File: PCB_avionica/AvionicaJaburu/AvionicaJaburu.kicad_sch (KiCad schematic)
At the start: 41 parts, among them J1 Screw_Terminal_01x02, J2 Screw_Terminal_01x02, J3 RESET, J4 Conn_01x08_Pin, J5 VDD, Q1 NMOS_Substrate, Q2 NMOS_Substrate, U1 AMS1117-3.3, U2 ESP32-DEVKIT-V1

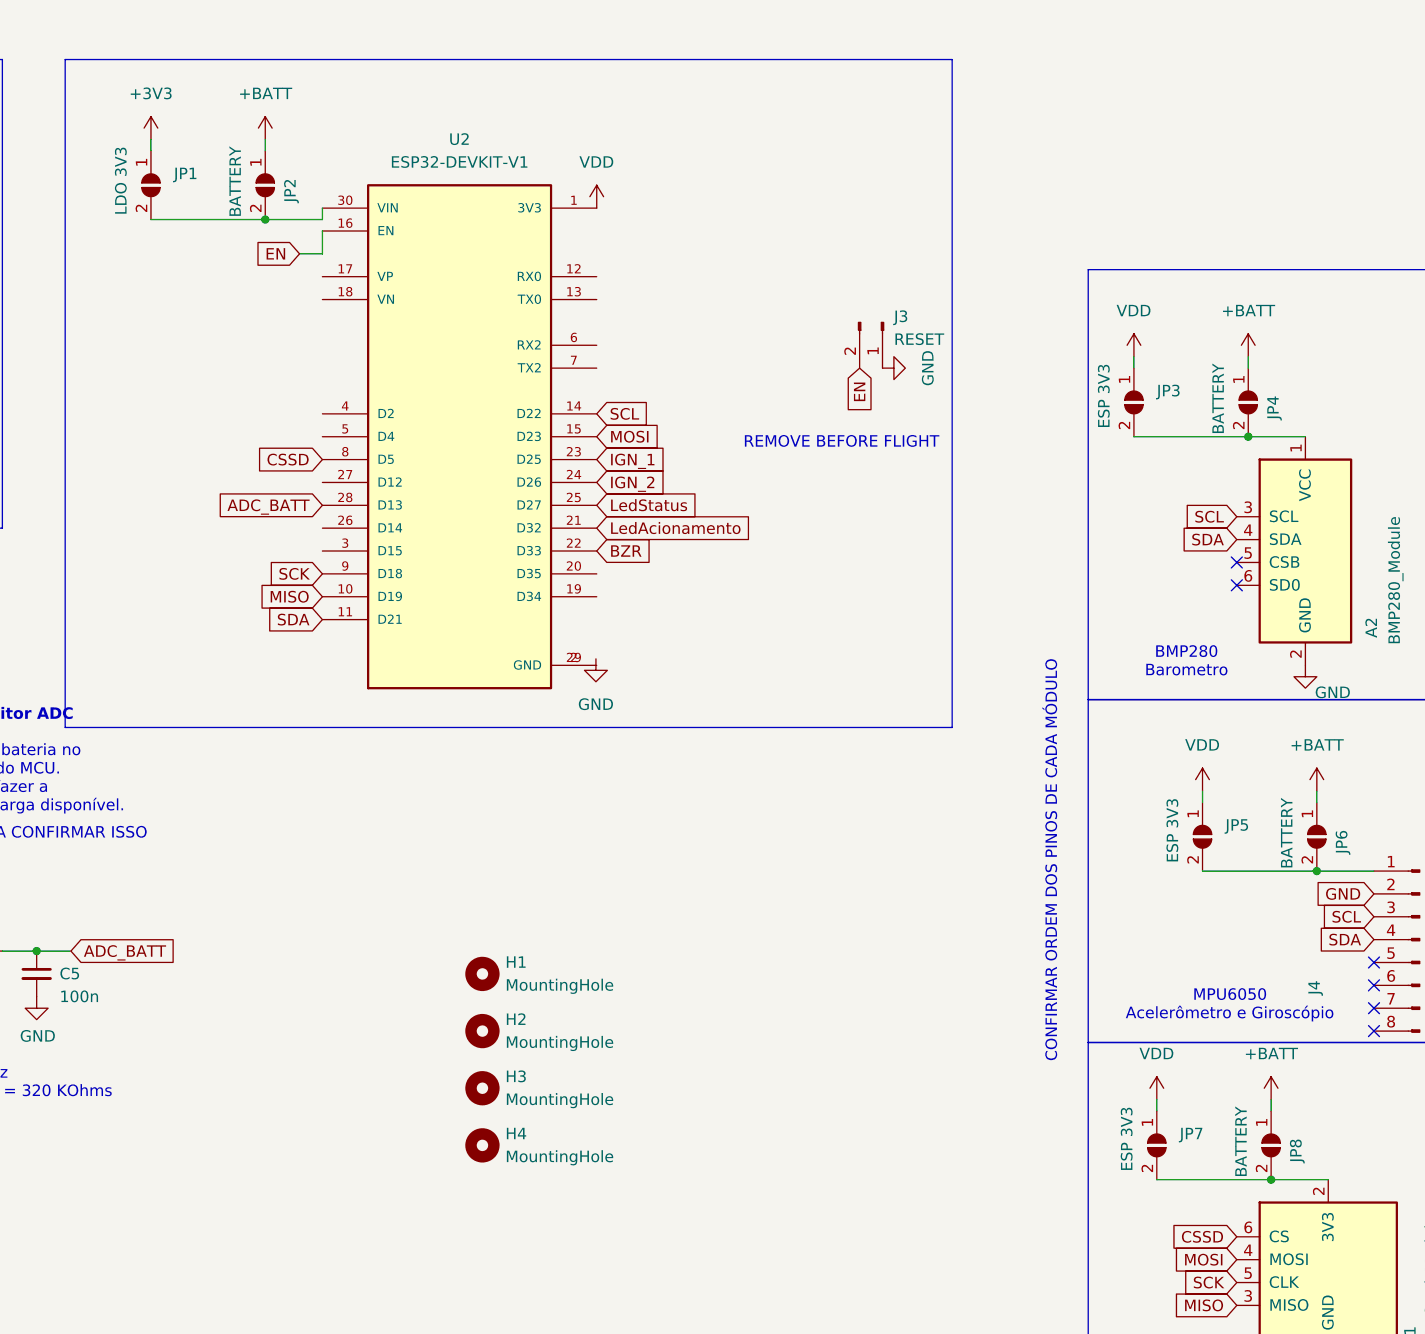
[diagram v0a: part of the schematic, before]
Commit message: outline da Jaburu corrigido pra fabricação
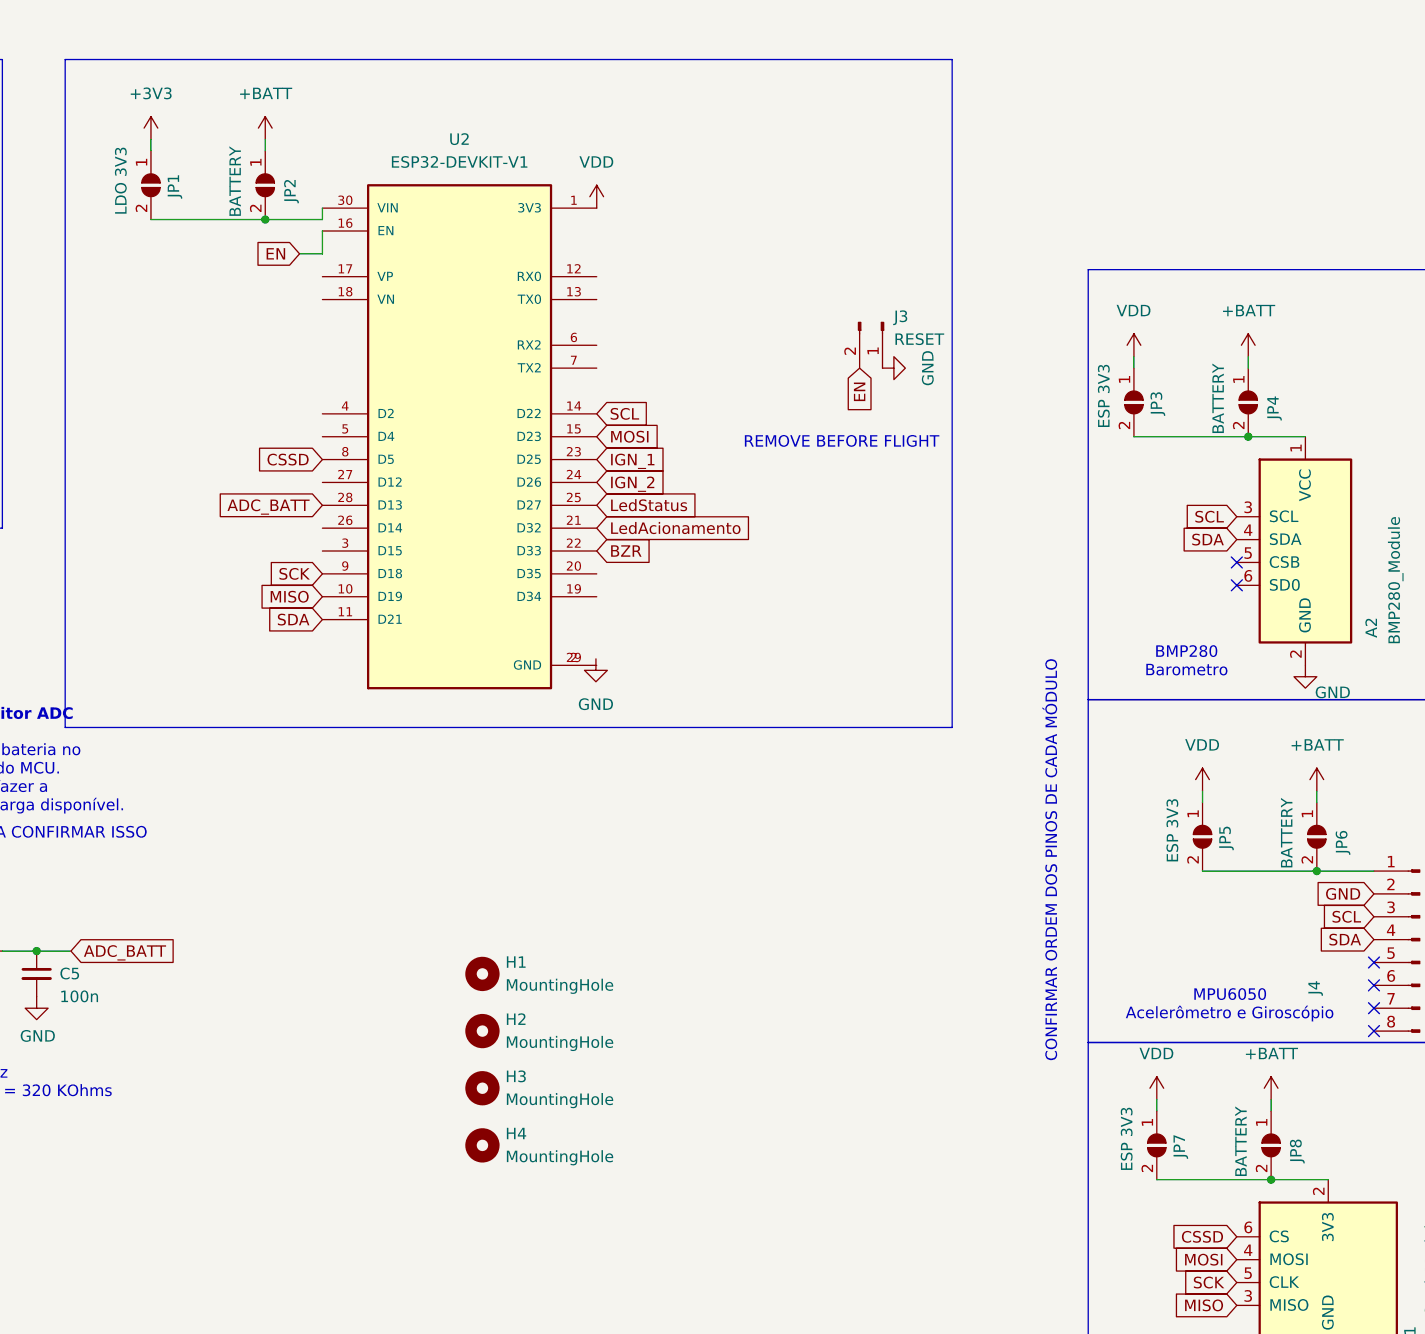
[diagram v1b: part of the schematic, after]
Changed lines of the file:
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@@
 		(dnp no)
 		(property "Reference" "JP7"
-			(at 250.19 132.0799 90)
+			(at 250.19 132.0799 0)
 			(effects
 				(font
@@
 		(dnp no)
 		(property "Reference" "JP1"
-			(at 138.43 25.3999 90)
+			(at 138.43 25.3999 0)
 			(effects
 				(font
@@
 		(dnp no)
 		(property "Reference" "JP3"
-			(at 247.65 49.5299 90)
+			(at 247.65 49.5299 0)
 			(effects
 				(font
@@
 		(dnp no)
 		(property "Reference" "JP5"
-			(at 255.27 97.7899 90)
+			(at 255.27 97.7899 0)
 			(effects
 				(font
